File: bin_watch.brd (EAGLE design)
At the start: 39.2 x 30.1 mm, 107 parts, among them J1 USB3100-XX-X_REVB, Q1 32.768kHz, T1 2N7002BKV, T2 2N7002BKV, T3 2N7002BKV, T4 2N7002BKV, T5 PMDT670UPE, T6 PMDT670UPE, T7 PMDT670UPE, U1 MCP73831T-2ACI/OT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

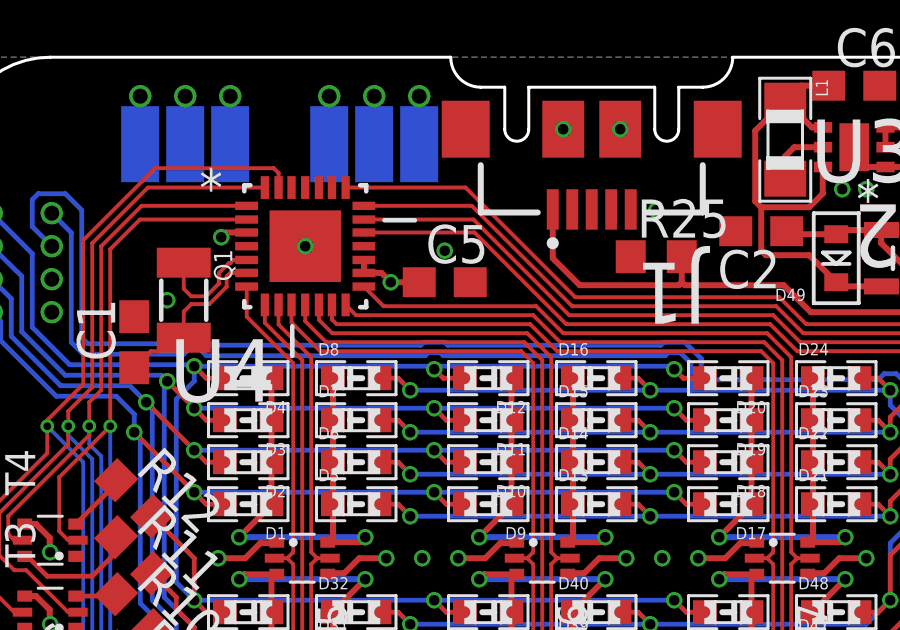
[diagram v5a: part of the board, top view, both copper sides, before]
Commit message: Vias on ISP lines
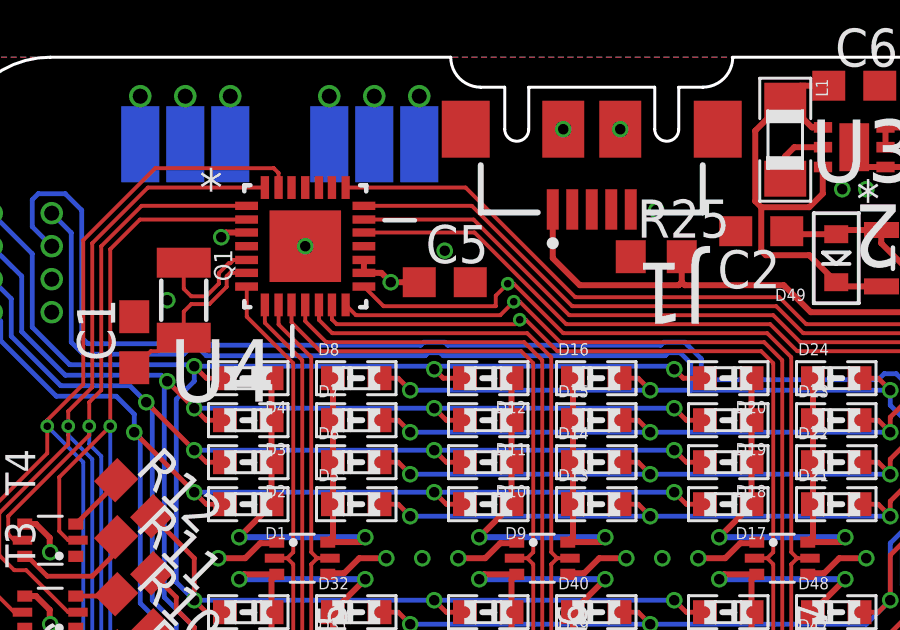
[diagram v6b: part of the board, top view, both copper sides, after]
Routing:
- net BLOCK1: track 39.9 -> 40.7 mm
- net G_BLOCK5: track 41.8 -> 42.7 mm, vias 2 -> 3
- net BTN3: track 35.8 -> 36.1 mm, vias 0 -> 1
- net G_BLOCK2: track 43.0 -> 43.1 mm, vias 2 -> 3
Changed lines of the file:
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@@
 <layers>
 <layer number="1" name="Top" color="23" fill="1" visible="yes" active="yes"/>
-<layer number="2" name="Route2" color="17" fill="1" visible="no" active="yes"/>
+<layer number="2" name="Route2" color="17" fill="1" visible="yes" active="yes"/>
 <layer number="3" name="Route3" color="4" fill="3" visible="no" active="no"/>
 <layer number="4" name="Route4" color="1" fill="4" visible="no" active="no"/>
@@
 <layer number="13" name="Route13" color="4" fill="5" visible="no" active="no"/>
 <layer number="14" name="Route14" color="1" fill="6" visible="no" active="no"/>
-<layer number="15" name="Route15" color="26" fill="1" visible="no" active="yes"/>
+<layer number="15" name="Route15" color="26" fill="1" visible="yes" active="yes"/>
 <layer number="16" name="Bottom" color="59" fill="1" visible="yes" active="yes"/>
 <layer number="17" name="Pads" color="2" fill="1" visible="yes" active="yes"/>
@@
 <layer number="47" name="Measures" color="7" fill="1" visible="no" active="yes"/>
 <layer number="48" name="Document" color="7" fill="1" visible="yes" active="yes"/>
-<layer number="49" name="Reference" color="7" fill="1" visible="no" active="yes"/>
+<layer number="49" name="Reference" color="7" fill="1" visible="yes" active="yes"/>
 <layer number="50" name="dxf" color="7" fill="1" visible="no" active="no"/>
 <layer number="51" name="tDocu" color="7" fill="1" visible="no" active="yes"/>
@@
 <contactref element="U4" pad="4"/>
 <contactref element="U4" pad="29"/>
-<via x="11.7" y="23.8" extent="1-16" drill="0.35"/>
+<via x="11.7" y="23.8" extent="1-16" drill="0.35" alwaysstop="yes"/>
 <via x="16.35" y="23.65" extent="1-16" drill="0.35"/>
 <via x="7.1" y="22" extent="1-16" drill="0.35"/>
@@
 <wire x1="9.2" y1="28.8" x2="9.2" y2="27.7" width="0.2" layer="2"/>
 <wire x1="9.85" y1="27.05" x2="14.05" y2="27.05" width="0.2" layer="2"/>
-<wire x1="14.05" y1="27.05" x2="18.1" y2="23" width="0.2" layer="2"/>
-<wire x1="18.1" y1="23" x2="22.1" y2="23" width="0.2" layer="2"/>
+<wire x1="14.05" y1="27.05" x2="15.4" y2="25.7" width="0.2" layer="2"/>
+<wire x1="15.4" y1="25.7" x2="19.4" y2="25.7" width="0.2" layer="2"/>
 <wire x1="25.5" y1="19.6" x2="25.5" y2="14.1" width="0.2" layer="2"/>
 <wire x1="9.2" y1="27.7" x2="9.85" y2="27.05" width="0.2" layer="2"/>
-<wire x1="22.1" y1="23" x2="25.5" y2="19.6" width="0.2" layer="2"/>
+<wire x1="19.4" y1="25.7" x2="25.5" y2="19.6" width="0.2" layer="2"/>
 </signal>
 <signal name="BLOCK3" class="3">
@@
 <wire x1="7.7" y1="27.2" x2="7.7" y2="28.8" width="0.2" layer="16"/>
 <via x="7.7" y="28.8" extent="1-16" drill="0.5" shape="square"/>
-<wire x1="17.5" y1="14.1" x2="17.5" y2="22.45" width="0.2" layer="2"/>
-<wire x1="17.5" y1="22.45" x2="13.7" y2="26.25" width="0.2" layer="2"/>
+<wire x1="17.5" y1="14.1" x2="17.5" y2="23.9" width="0.2" layer="2"/>
+<wire x1="17.5" y1="23.9" x2="16.5" y2="24.9" width="0.2" layer="2"/>
+<wire x1="16.5" y1="24.9" x2="15.05" y2="24.9" width="0.2" layer="2"/>
+<wire x1="15.05" y1="24.9" x2="13.7" y2="26.25" width="0.2" layer="2"/>
 <wire x1="13.7" y1="26.25" x2="9.1" y2="26.25" width="0.2" layer="2"/>
 <wire x1="9.1" y1="26.25" x2="7.7" y2="27.65" width="0.2" layer="2"/>
@@
 <wire x1="27.6" y1="20" x2="27.6" y2="5.3" width="0.13" layer="1"/>
 <wire x1="27" y1="20.6" x2="27.6" y2="20" width="0.13" layer="1"/>
-<wire x1="19.3" y1="21.5" x2="20.2" y2="20.6" width="0.13" layer="1"/>
+<wire x1="20.2" y1="20.6" x2="18.85" y2="21.95" width="0.13" layer="1"/>
 <wire x1="20.2" y1="20.6" x2="27" y2="20.6" width="0.13" layer="1"/>
 <contactref element="U4" pad="14"/>
 <wire x1="13.0462" y1="21.8442" x2="13.3904" y2="21.5" width="0.13" layer="1"/>
-<wire x1="13.3904" y1="21.5" x2="19.3" y2="21.5" width="0.13" layer="1"/>
+<wire x1="18.2" y1="21.5" x2="13.3904" y2="21.5" width="0.13" layer="1"/>
+<wire x1="18.85" y1="21.95" x2="18.65" y2="21.95" width="0.13" layer="1"/>
+<via x="18.65" y="21.95" extent="1-16" drill="0.254"/>
+<wire x1="18.65" y1="21.95" x2="18.2" y2="21.5" width="0.13" layer="1"/>
 </signal>
 <signal name="VCC" class="1">
@@
 <contactref element="T7" pad="2"/>
 <wire x1="26.9" y1="20.3" x2="20.1" y2="20.3" width="0.13" layer="1"/>
-<wire x1="19.2" y1="21.2" x2="20.1" y2="20.3" width="0.13" layer="1"/>
 <contactref element="R21" pad="1"/>
 <wire x1="36.401040625" y1="2.89895625" x2="37.1" y2="2.2" width="0.13" layer="1"/>
@@
 <wire x1="12.589" y1="21.8442" x2="12.589" y2="21.361" width="0.13" layer="1"/>
 <wire x1="12.589" y1="21.361" x2="12.75" y2="21.2" width="0.13" layer="1"/>
-<wire x1="12.75" y1="21.2" x2="19.2" y2="21.2" width="0.13" layer="1"/>
+<wire x1="18.85" y1="21.35" x2="19.05" y2="21.35" width="0.13" layer="1"/>
+<via x="18.85" y="21.35" extent="1-16" drill="0.254"/>
+<wire x1="20.1" y1="20.3" x2="19.05" y2="21.35" width="0.13" layer="1"/>
+<wire x1="12.75" y1="21.2" x2="18.7" y2="21.2" width="0.13" layer="1"/>
+<wire x1="18.7" y1="21.2" x2="18.85" y2="21.35" width="0.13" layer="1"/>
 </signal>
 <signal name="G_BLOCK3" class="4">
@@
 <wire x1="27.1" y1="20.9" x2="27.9" y2="20.1" width="0.13" layer="1"/>
 <contactref element="T7" pad="5"/>
-<wire x1="20.3" y1="20.9" x2="19.4" y2="21.8" width="0.13" layer="1"/>
+<wire x1="18.65" y1="22.55" x2="20.3" y2="20.9" width="0.13" layer="1"/>
 <wire x1="20.3" y1="20.9" x2="27.1" y2="20.9" width="0.13" layer="1"/>
 <contactref element="R24" pad="1"/>
@@
 <wire x1="31.4" y1="3.2" x2="38.1" y2="3.2" width="0.13" layer="16"/>
 <contactref element="U4" pad="15"/>
-<wire x1="14.3096" y1="21.8" x2="13.6558" y2="22.4538" width="0.13" layer="1"/>
-<wire x1="19.4" y1="21.8" x2="14.3096" y2="21.8" width="0.13" layer="1"/>
+<wire x1="13.6558" y1="22.4538" x2="14.3096" y2="21.8" width="0.13" layer="1"/>
+<wire x1="18.65" y1="22.55" x2="18.45" y2="22.55" width="0.13" layer="1"/>
+<via x="18.45" y="22.55" extent="1-16" drill="0.254"/>
+<wire x1="18.05" y1="21.8" x2="14.3096" y2="21.8" width="0.13" layer="1"/>
+<wire x1="18.45" y1="22.55" x2="18.05" y2="22.15" width="0.13" layer="1"/>
+<wire x1="18.05" y1="22.15" x2="18.05" y2="21.8" width="0.13" layer="1"/>
 </signal>
 <signal name="G_LIGHT0" class="4">

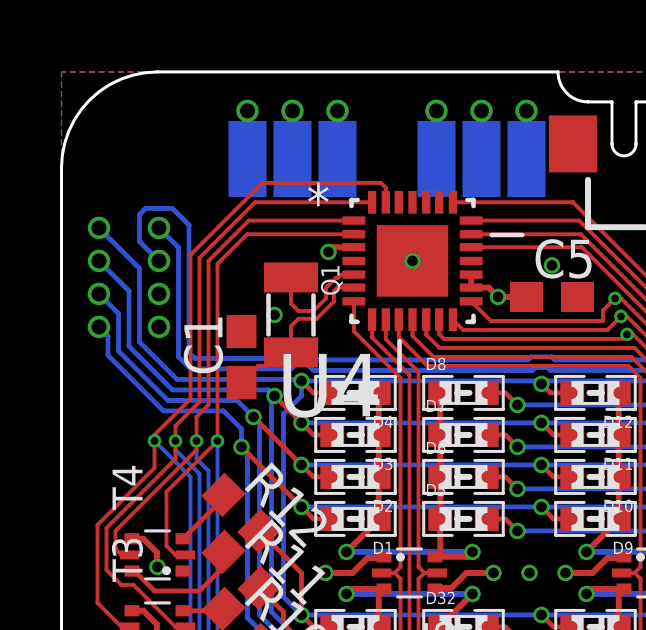
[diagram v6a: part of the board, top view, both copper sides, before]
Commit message: Gap between row solderpads reduced
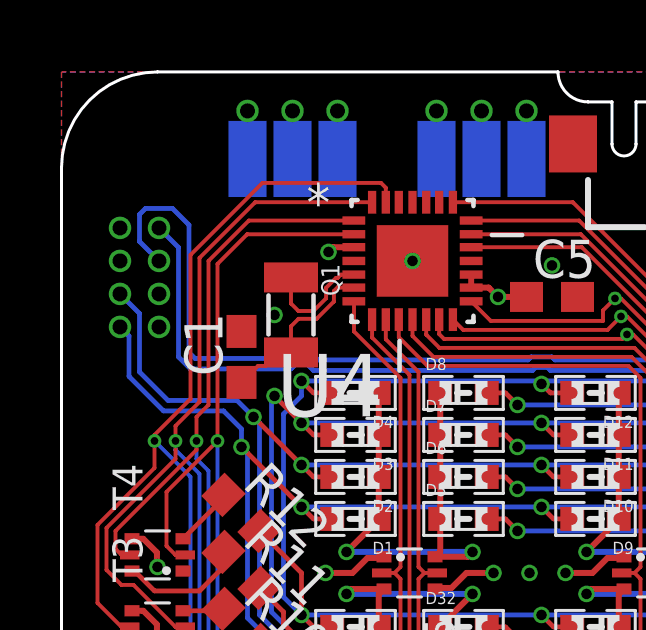
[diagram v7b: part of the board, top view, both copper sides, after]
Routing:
- net LIGHT6: track 61.3 -> 61.8 mm
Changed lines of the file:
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@@
 <wire x1="6.601040625" y1="10.99895625" x2="8" y2="9.599996875" width="0.16" layer="1"/>
 <wire x1="8" y1="9.599996875" x2="8" y2="9.2" width="0.16" layer="1"/>
-<via x="1.25" y="22.7" extent="1-16" drill="0.5" shape="square"/>
+<via x="1.95" y="22.7" extent="1-16" drill="0.5" shape="square"/>
 <wire x1="6.4" y1="18.6" x2="5.85" y2="19.15" width="0.16" layer="16"/>
 <wire x1="5.85" y1="19.15" x2="3.55" y2="19.15" width="0.16" layer="16"/>
-<wire x1="3.55" y1="19.15" x2="1.9" y2="20.8" width="0.16" layer="16"/>
-<wire x1="1.9" y1="20.8" x2="1.9" y2="22.05" width="0.16" layer="16"/>
-<wire x1="1.9" y1="22.05" x2="1.25" y2="22.7" width="0.16" layer="16"/>
+<wire x1="3.55" y1="19.15" x2="2.6" y2="20.1" width="0.16" layer="16"/>
+<wire x1="2.6" y1="20.1" x2="2.6" y2="22.05" width="0.16" layer="16"/>
+<wire x1="2.6" y1="22.05" x2="1.95" y2="22.7" width="0.16" layer="16"/>
 </signal>
 <signal name="LIGHT6">
@@
 <wire x1="7.4" y1="11.7" x2="7.4" y2="12.099996875" width="0.16" layer="1"/>
 <wire x1="7.4" y1="12.099996875" x2="6.601040625" y2="12.89895625" width="0.16" layer="1"/>
-<via x="1.25" y="23.8" extent="1-16" drill="0.5" shape="square"/>
-<wire x1="7.1" y1="19.3" x2="6.9" y2="19.5" width="0.16" layer="16"/>
-<wire x1="6.9" y1="19.5" x2="3.7" y2="19.5" width="0.16" layer="16"/>
-<wire x1="3.7" y1="19.5" x2="2.25" y2="20.95" width="0.16" layer="16"/>
-<wire x1="1.25" y1="23.7894125" x2="1.25" y2="23.8" width="0.16" layer="16"/>
-<wire x1="2.25" y1="20.95" x2="2.25" y2="22.8" width="0.16" layer="16"/>
-<wire x1="2.25" y1="22.8" x2="1.25" y2="23.7894125" width="0.16" layer="16"/>
+<via x="1.95" y="23.8" extent="1-16" drill="0.5" shape="square"/>
+<wire x1="1.95" y1="23.7894125" x2="1.95" y2="23.8" width="0.16" layer="16"/>
+<wire x1="1.95" y1="23.8" x2="1.3" y2="23.15" width="0.16" layer="2"/>
+<wire x1="6.75" y1="19.65" x2="7.1" y2="19.3" width="0.16" layer="2"/>
+<wire x1="1.3" y1="23.15" x2="1.3" y2="21.35" width="0.16" layer="2"/>
+<wire x1="1.3" y1="21.35" x2="3" y2="19.65" width="0.16" layer="2"/>
+<wire x1="3" y1="19.65" x2="6.75" y2="19.65" width="0.16" layer="2"/>
 </signal>
 <signal name="LIGHT7">
@@
 <wire x1="6.601040625" y1="14.79895625" x2="8" y2="13.399996875" width="0.16" layer="1"/>
 <wire x1="8" y1="13.399996875" x2="8" y2="12" width="0.16" layer="1"/>
-<via x="1.25" y="24.9" extent="1-16" drill="0.5" shape="square"/>
-<wire x1="8" y1="19.8" x2="7.95" y2="19.85" width="0.16" layer="16"/>
-<wire x1="7.95" y1="19.85" x2="3.85" y2="19.85" width="0.16" layer="16"/>
-<wire x1="3.85" y1="19.85" x2="2.6" y2="21.1" width="0.16" layer="16"/>
-<wire x1="2.6" y1="21.1" x2="2.6" y2="23.55" width="0.16" layer="16"/>
-<wire x1="2.6" y1="23.55" x2="1.25" y2="24.9" width="0.16" layer="16"/>
+<via x="1.95" y="24.9" extent="1-16" drill="0.5" shape="square"/>
+<wire x1="8" y1="19.8" x2="7.8" y2="20" width="0.16" layer="2"/>
+<wire x1="3.65" y1="20" x2="2.6" y2="21.05" width="0.16" layer="2"/>
+<wire x1="2.6" y1="21.05" x2="2.6" y2="24.25" width="0.16" layer="2"/>
+<wire x1="2.6" y1="24.25" x2="1.95" y2="24.9" width="0.16" layer="2"/>
+<wire x1="7.8" y1="20" x2="3.65" y2="20" width="0.16" layer="2"/>
 </signal>
 <signal name="BLOCK0" class="3">
@@
 <wire x1="8" y1="7.8" x2="7.899996875" y2="7.8" width="0.16" layer="1"/>
 <wire x1="7.899996875" y1="7.8" x2="6.601040625" y2="9.09895625" width="0.16" layer="1"/>
-<via x="1.25" y="21.6" extent="1-16" drill="0.5" shape="square"/>
-<wire x1="1.25" y1="21.6" x2="1.55" y2="21.3" width="0.16" layer="16"/>
-<wire x1="1.55" y1="21.3" x2="1.55" y2="20.65" width="0.16" layer="16"/>
-<wire x1="1.55" y1="20.65" x2="3.4" y2="18.8" width="0.16" layer="16"/>
+<via x="1.95" y="21.6" extent="1-16" drill="0.5" shape="square"/>
+<wire x1="1.95" y1="21.6" x2="2.25" y2="21.3" width="0.16" layer="16"/>
+<wire x1="2.25" y1="21.3" x2="2.25" y2="19.95" width="0.16" layer="16"/>
+<wire x1="2.25" y1="19.95" x2="3.4" y2="18.8" width="0.16" layer="16"/>
 <wire x1="3.4" y1="18.8" x2="5.4" y2="18.8" width="0.16" layer="16"/>
 <wire x1="5.4" y1="18.8" x2="6" y2="18.2" width="0.16" layer="16"/>

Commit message: Assortment of tiny tweaks
Made some wires closer together, and other stuff I forgot
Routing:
- net GND: track 8.31 -> 9.06 mm
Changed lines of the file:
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@@
 <layer number="19" name="Unrouted" color="6" fill="1" visible="yes" active="yes"/>
 <layer number="20" name="Dimension" color="15" fill="1" visible="yes" active="yes"/>
-<layer number="21" name="tPlace" color="7" fill="1" visible="no" active="yes"/>
+<layer number="21" name="tPlace" color="7" fill="1" visible="yes" active="yes"/>
 <layer number="22" name="bPlace" color="7" fill="1" visible="no" active="yes"/>
 <layer number="23" name="tOrigins" color="15" fill="1" visible="yes" active="yes"/>
@@
 <layer number="49" name="Reference" color="7" fill="1" visible="yes" active="yes"/>
 <layer number="50" name="dxf" color="7" fill="1" visible="no" active="no"/>
-<layer number="51" name="tDocu" color="7" fill="1" visible="no" active="yes"/>
+<layer number="51" name="tDocu" color="7" fill="1" visible="yes" active="yes"/>
 <layer number="52" name="bDocu" color="7" fill="1" visible="no" active="yes"/>
 <layer number="53" name="tGND_GNDA" color="7" fill="9" visible="no" active="no"/>
@@
 <wire x1="2.25" y1="28.05" x2="2.25" y2="27.55" width="0.06" layer="22"/>
 <wire x1="2.25" y1="26.45" x2="2.25" y2="26.95" width="0.06" layer="22"/>
-<circle x="13.8" y="27.15" radius="0.05" width="0.06" layer="48"/>
+<circle x="9.75" y="25.75" radius="0.05" width="0.06" layer="48"/>
 <circle x="31.35" y="25.7" radius="0.05" width="0.06" layer="48"/>
 <wire x1="29.4" y1="23.3" x2="29.2" y2="23.5" width="0.06" layer="48"/>
@@
 <element name="PAD13" library="wirepad" library_urn="urn:adsk.eagle:library:412" package="SMD1,27-2,54" package3d_urn="urn:adsk.eagle:package:30839/1" value="" x="14" y="27.2" rot="MR0"/>
 <element name="PAD14" library="wirepad" library_urn="urn:adsk.eagle:library:412" package="SMD1,27-2,54" package3d_urn="urn:adsk.eagle:package:30839/1" value="" x="15.5" y="27.2" rot="MR180"/>
-<element name="C5" library="rcl" library_urn="urn:adsk.eagle:library:334" package="C0603" package3d_urn="urn:adsk.eagle:package:23616/2" value="47u" x="16.35" y="22.6"/>
+<element name="C5" library="rcl" library_urn="urn:adsk.eagle:library:334" package="C0603" package3d_urn="urn:adsk.eagle:package:23616/2" value="47u" x="16.4" y="22.6"/>
 <element name="R25" library="rcl" library_urn="urn:adsk.eagle:library:334" package="R0603" package3d_urn="urn:adsk.eagle:package:23555/1" value="1M" x="23.4" y="23.45"/>
 <element name="U4" library="Atmel_By_element14_Batch_1-00" package="QFN45P400X400X100-29N" value="ATMEGA48PA-MMH" x="11.7" y="23.8">
@@
 <contactref element="U4" pad="29"/>
 <via x="11.7" y="23.8" extent="1-16" drill="0.35" alwaysstop="yes"/>
-<via x="16.35" y="23.65" extent="1-16" drill="0.35"/>
+<via x="14.6" y="23.7" extent="1-16" drill="0.35"/>
 <via x="7.1" y="22" extent="1-16" drill="0.35"/>
+<wire x1="3.39895625" y1="6.69895625" x2="3.39895625" y2="7.09895625" width="0.2" layer="1"/>
+<wire x1="3.39895625" y1="7.09895625" x2="3.65" y2="7.35" width="0.2" layer="1"/>
 </signal>
 <signal name="XTAL_N" class="4">
@@
 <via x="14.55" y="22.6" extent="1-16" drill="0.35"/>
 <wire x1="14.239" y1="22.911" x2="14.55" y2="22.6" width="0.2" layer="1"/>
-<wire x1="14.55" y1="22.6" x2="15.5" y2="22.6" width="0.2" layer="1"/>
+<wire x1="14.55" y1="22.6" x2="15.55" y2="22.6" width="0.2" layer="1"/>
 </signal>
 <signal name="G_BLOCK0" class="4">
@@
 <wire x1="18.65" y1="22.55" x2="18.45" y2="22.55" width="0.13" layer="1"/>
 <via x="18.45" y="22.55" extent="1-16" drill="0.254"/>
-<wire x1="18.05" y1="21.8" x2="14.3096" y2="21.8" width="0.13" layer="1"/>
-<wire x1="18.45" y1="22.55" x2="18.05" y2="22.15" width="0.13" layer="1"/>
-<wire x1="18.05" y1="22.15" x2="18.05" y2="21.8" width="0.13" layer="1"/>
+<wire x1="18.1" y1="21.8" x2="14.3096" y2="21.8" width="0.13" layer="1"/>
+<wire x1="18.45" y1="22.55" x2="18.1" y2="22.2" width="0.13" layer="1"/>
+<wire x1="18.1" y1="22.2" x2="18.1" y2="21.8" width="0.13" layer="1"/>
 </signal>
 <signal name="G_LIGHT0" class="4">
@@
 <wire x1="33.95" y1="7.6" x2="32.9" y2="7.6" width="0.13" layer="16"/>
 <contactref element="U4" pad="21"/>
-<wire x1="13.6558" y1="25.1462" x2="17.2538" y2="25.1462" width="0.13" layer="1"/>
-<wire x1="17.2538" y1="25.1462" x2="20.6" y2="21.8" width="0.13" layer="1"/>
+<wire x1="13.6558" y1="25.1462" x2="14.2538" y2="25.1462" width="0.13" layer="1"/>
+<wire x1="14.2538" y1="25.1462" x2="14.55" y2="24.85" width="0.13" layer="1"/>
+<wire x1="14.55" y1="24.85" x2="17.55" y2="24.85" width="0.13" layer="1"/>
+<wire x1="17.55" y1="24.85" x2="20.6" y2="21.8" width="0.13" layer="1"/>
 </signal>
 <signal name="G_LIGHT1" class="4">
@@
 <wire x1="33.35" y1="6.6" x2="31.9" y2="6.6" width="0.13" layer="16"/>
 <contactref element="U4" pad="22"/>
-<wire x1="13.0462" y1="25.7558" x2="17.0442" y2="25.7558" width="0.13" layer="1"/>
-<wire x1="17.0442" y1="25.7558" x2="20.7" y2="22.1" width="0.13" layer="1"/>
+<wire x1="13.0462" y1="25.7558" x2="14.0442" y2="25.7558" width="0.13" layer="1"/>
+<wire x1="14.0442" y1="25.7558" x2="14.65" y2="25.15" width="0.13" layer="1"/>
+<wire x1="14.65" y1="25.15" x2="17.65" y2="25.15" width="0.13" layer="1"/>
+<wire x1="17.65" y1="25.15" x2="20.7" y2="22.1" width="0.13" layer="1"/>
 </signal>
 <signal name="G_LIGHT2" class="4">
@@
 <wire x1="34.55" y1="8.6" x2="33.9" y2="8.6" width="0.13" layer="16"/>
 <contactref element="U4" pad="20"/>
-<wire x1="13.6558" y1="24.689" x2="17.311" y2="24.689" width="0.13" layer="1"/>
-<wire x1="17.311" y1="24.689" x2="20.5" y2="21.5" width="0.13" layer="1"/>
+<wire x1="13.6558" y1="24.689" x2="14.311" y2="24.689" width="0.13" layer="1"/>
+<wire x1="14.311" y1="24.689" x2="14.45" y2="24.55" width="0.13" layer="1"/>
+<wire x1="14.45" y1="24.55" x2="17.45" y2="24.55" width="0.13" layer="1"/>
+<wire x1="17.45" y1="24.55" x2="20.5" y2="21.5" width="0.13" layer="1"/>
 </signal>
 <signal name="G_LIGHT4" class="4">
@@
 <wire x1="4.3" y1="16.6" x2="3.1" y2="17.8" width="0.13" layer="16"/>
 <contactref element="U4" pad="27"/>
-<wire x1="4.3" y1="24" x2="6.7" y2="26.4" width="0.13" layer="1"/>
-<wire x1="10.65" y1="26.4" x2="10.811" y2="26.239" width="0.13" layer="1"/>
+<wire x1="4.3" y1="24" x2="6.65" y2="26.35" width="0.13" layer="1"/>
+<wire x1="10.7" y1="26.35" x2="10.811" y2="26.239" width="0.13" layer="1"/>
 <wire x1="10.811" y1="26.239" x2="10.811" y2="25.7558" width="0.13" layer="1"/>
-<wire x1="6.7" y1="26.4" x2="10.65" y2="26.4" width="0.13" layer="1"/>
+<wire x1="6.65" y1="26.35" x2="10.7" y2="26.35" width="0.13" layer="1"/>
 </signal>
 <signal name="G_LIGHT6" class="4">
